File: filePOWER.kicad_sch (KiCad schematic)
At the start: 35 parts, among them U1 FAN53541, U10 NCP115-2.5, U15 TUSB320L, U2 FAN53541, U7 AP22816BKB

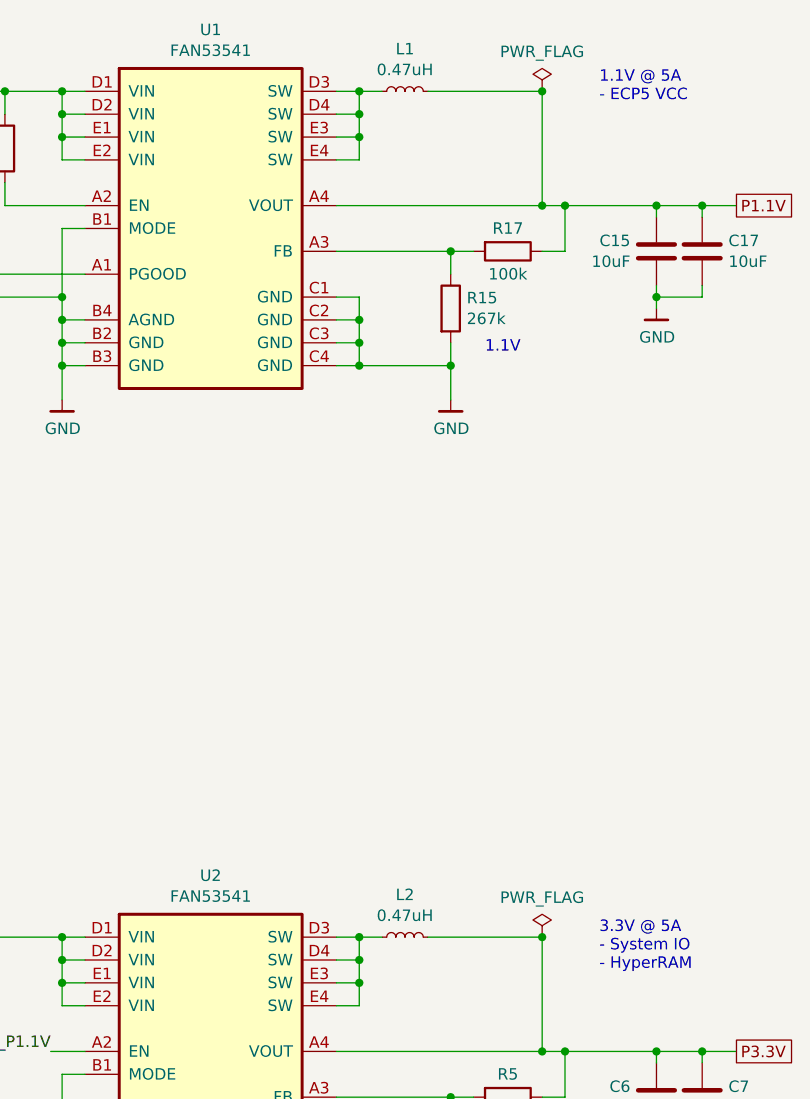
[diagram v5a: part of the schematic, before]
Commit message: Convert to KiCAD 7
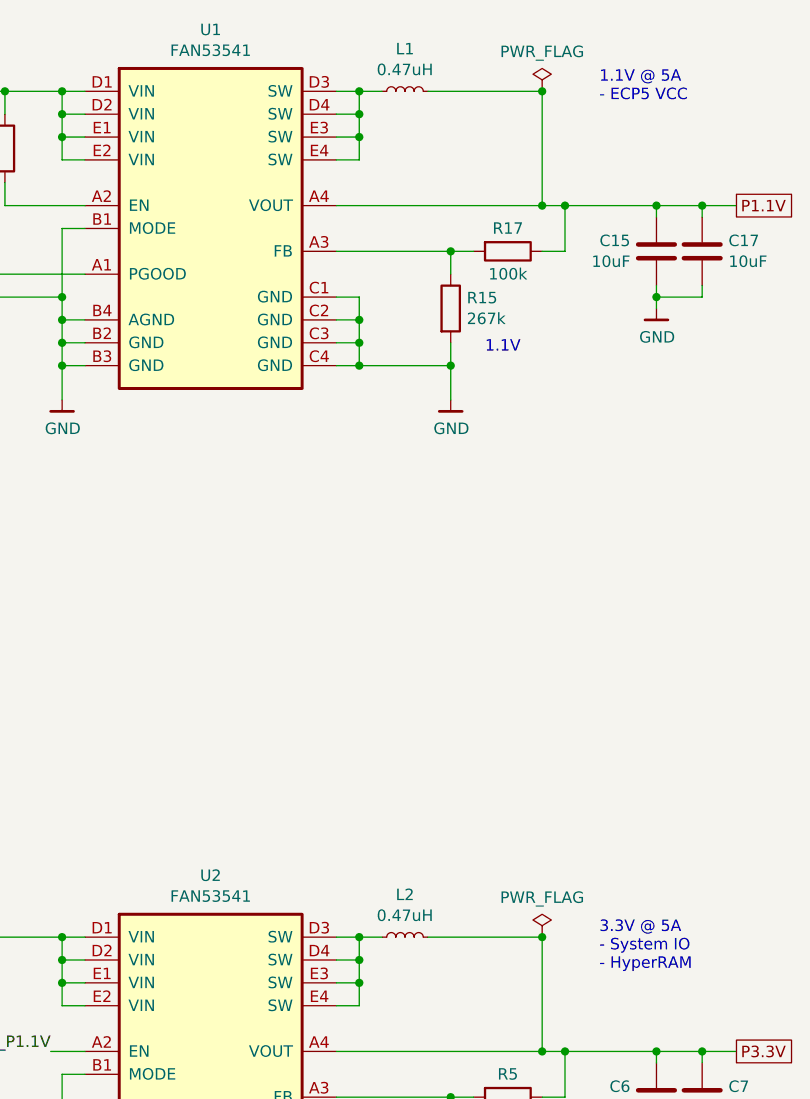
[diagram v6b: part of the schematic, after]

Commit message: Update component prices
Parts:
- C1, C12, C46, C47, C77: Pricing (EUR) 0,17 -> 0,14
- C15, C17, C6, C7: Pricing (EUR) 0,18 -> 0,14
- C2, C5: Pricing (EUR) 0,09 -> 0,08
- C3: Pricing (EUR) 0,18 -> 0,15
- L1, L2: Pricing (EUR) 0,28 -> 0,20
- R1, R13, R15, R17, R2, R25, R5: Pricing (EUR) 0,11 -> 0,09
- R14, R18: Pricing (EUR) 0,10 -> 0,09
- U10: Pricing (EUR) 0,49 -> 0,35
- U15: Pricing (EUR) 2,05 -> 1,79
- U7: Pricing (EUR) 0,44 -> 0,41
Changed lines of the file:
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@@
       (effects (font (size 1.27 1.27)) hide)
     )
-    (property "Pricing (EUR)" "0,28" (at 234.95 124.46 0)
+    (property "Pricing (EUR)" "0,20" (at 234.95 124.46 0)
       (effects (font (size 1.27 1.27)) hide)
     )
@@
       (effects (font (size 1.27 1.27)) hide)
     )
-    (property "Pricing (EUR)" "0,11" (at 240.03 148.59 0)
+    (property "Pricing (EUR)" "0,09" (at 240.03 148.59 0)
       (effects (font (size 1.27 1.27)) hide)
     )
@@
       (effects (font (size 1.27 1.27)) hide)
     )
-    (property "Pricing (EUR)" "0,11" (at 246.38 142.24 0)
+    (property "Pricing (EUR)" "0,09" (at 246.38 142.24 0)
       (effects (font (size 1.27 1.27)) hide)
     )
@@
       (effects (font (size 1.27 1.27)) hide)
     )
-    (property "Pricing (EUR)" "0,18" (at 262.89 142.24 0)
+    (property "Pricing (EUR)" "0,14" (at 262.89 142.24 0)
       (effects (font (size 1.27 1.27)) hide)
     )
@@
       (effects (font (size 1.27 1.27)) hide)
     )
-    (property "Pricing (EUR)" "0,18" (at 267.97 142.24 0)
+    (property "Pricing (EUR)" "0,14" (at 267.97 142.24 0)
       (effects (font (size 1.27 1.27)) hide)
     )
@@
       (effects (font (size 1.27 1.27)) hide)
     )
-    (property "Pricing (EUR)" "0,11" (at 167.64 134.62 0)
+    (property "Pricing (EUR)" "0,09" (at 167.64 134.62 0)
       (effects (font (size 1.27 1.27)) hide)
     )
@@
       (effects (font (size 1.27 1.27)) hide)
     )
-    (property "Pricing (EUR)" "0,09" (at 177.8 129.54 0)
+    (property "Pricing (EUR)" "0,08" (at 177.8 129.54 0)
       (effects (font (size 1.27 1.27)) hide)
     )
@@
       (effects (font (size 1.27 1.27)) hide)
     )
-    (property "Pricing (EUR)" "0,17" (at 115.57 40.64 0)
+    (property "Pricing (EUR)" "0,14" (at 115.57 40.64 0)
       (effects (font (size 1.27 1.27)) hide)
     )
@@
       (effects (font (size 1.27 1.27)) hide)
     )
-    (property "Pricing (EUR)" "0,28" (at 234.95 30.48 0)
+    (property "Pricing (EUR)" "0,20" (at 234.95 30.48 0)
       (effects (font (size 1.27 1.27)) hide)
     )
@@
       (effects (font (size 1.27 1.27)) hide)
     )
-    (property "Pricing (EUR)" "0,11" (at 240.03 54.61 0)
+    (property "Pricing (EUR)" "0,09" (at 240.03 54.61 0)
       (effects (font (size 1.27 1.27)) hide)
     )
@@
       (effects (font (size 1.27 1.27)) hide)
     )
-    (property "Pricing (EUR)" "0,11" (at 246.38 48.26 0)
+    (property "Pricing (EUR)" "0,09" (at 246.38 48.26 0)
       (effects (font (size 1.27 1.27)) hide)
     )
@@
       (effects (font (size 1.27 1.27)) hide)
     )
-    (property "Pricing (EUR)" "0,18" (at 262.89 48.26 0)
+    (property "Pricing (EUR)" "0,14" (at 262.89 48.26 0)
       (effects (font (size 1.27 1.27)) hide)
     )
@@
       (effects (font (size 1.27 1.27)) hide)
     )
-    (property "Pricing (EUR)" "0,18" (at 267.97 48.26 0)
+    (property "Pricing (EUR)" "0,14" (at 267.97 48.26 0)
       (effects (font (size 1.27 1.27)) hide)
     )
@@
       (effects (font (size 1.27 1.27)) hide)
     )
-    (property "Pricing (EUR)" "0,11" (at 158.75 40.64 0)
+    (property "Pricing (EUR)" "0,09" (at 158.75 40.64 0)
       (effects (font (size 1.27 1.27)) hide)
     )
@@
       (effects (font (size 1.27 1.27)) hide)
     )
-    (property "Pricing (EUR)" "0,18" (at 168.91 35.56 0)
+    (property "Pricing (EUR)" "0,15" (at 168.91 35.56 0)
       (effects (font (size 1.27 1.27)) hide)
     )
@@
       (effects (font (size 1.27 1.27)) hide)
     )
-    (property "Pricing (EUR)" "0,09" (at 175.26 35.56 0)
+    (property "Pricing (EUR)" "0,08" (at 175.26 35.56 0)
       (effects (font (size 1.27 1.27)) hide)
     )
@@
       (effects (font (size 1.27 1.27)) hide)
     )
-    (property "Pricing (EUR)" "0,17" (at 30.48 39.37 0)
+    (property "Pricing (EUR)" "0,14" (at 30.48 39.37 0)
       (effects (font (size 1.27 1.27)) hide)
     )
@@
       (effects (font (size 1.27 1.27)) hide)
     )
-    (property "Pricing (EUR)" "0,49" (at 88.011 146.812 0)
+    (property "Pricing (EUR)" "0,35" (at 88.011 146.812 0)
       (effects (font (size 1.27 1.27)) hide)
     )
@@
       (effects (font (size 1.27 1.27)) hide)
     )
-    (property "Pricing (EUR)" "0,17" (at 58.801 149.352 0)
+    (property "Pricing (EUR)" "0,14" (at 58.801 149.352 0)
       (effects (font (size 1.27 1.27)) hide)
     )
@@
       (effects (font (size 1.27 1.27)) hide)
     )
-    (property "Pricing (EUR)" "0,17" (at 107.061 149.352 0)
+    (property "Pricing (EUR)" "0,14" (at 107.061 149.352 0)
       (effects (font (size 1.27 1.27)) hide)
     )
@@
       (effects (font (size 1.27 1.27)) hide)
     )
-    (property "Pricing (EUR)" "0,11" (at 190.5 36.83 0)
+    (property "Pricing (EUR)" "0,09" (at 190.5 36.83 0)
       (effects (font (size 1.27 1.27)) hide)
     )
@@
       (effects (font (size 1.27 1.27)) hide)
     )
-    (property "Pricing (EUR)" "0,17" (at 30.48 70.485 0)
+    (property "Pricing (EUR)" "0,14" (at 30.48 70.485 0)
       (effects (font (size 1.27 1.27)) hide)
     )
@@
       (effects (font (size 1.27 1.27)) hide)
     )
-    (property "Pricing (EUR)" "2,05" (at 65.405 101.727 0)
+    (property "Pricing (EUR)" "1,79" (at 65.405 101.727 0)
       (effects (font (size 1.27 1.27)) hide)
     )
@@
       (effects (font (size 1.27 1.27)) hide)
     )
-    (property "Pricing (EUR)" "0,10" (at 88.265 94.107 0)
+    (property "Pricing (EUR)" "0,09" (at 88.265 94.107 0)
       (effects (font (size 1.27 1.27)) hide)
     )
@@
       (effects (font (size 1.27 1.27)) hide)
     )
-    (property "Pricing (EUR)" "0,10" (at 60.96 75.565 0)
+    (property "Pricing (EUR)" "0,09" (at 60.96 75.565 0)
       (effects (font (size 1.27 1.27)) hide)
     )
@@
       (effects (font (size 1.27 1.27)) hide)
     )
-    (property "Pricing (EUR)" "0,44" (at 53.975 51.435 0)
-      (effects (font (size 1.27 1.27)) hide)
-    )
+    (property "Pricing (EUR)" "0,41" (at 53.975 51.435 0)
+      (effects (font (size 1.27 1.27)) hide)
+    )
